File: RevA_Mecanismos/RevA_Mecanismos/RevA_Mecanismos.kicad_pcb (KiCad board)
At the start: 4 copper layers, 99.7 x 99.7 mm, 137 parts, among them IC1 MAX33040EAKA+T, J1 Conn_01x02_Socket, J10 Screw_Terminal_01x02, J11 Screw_Terminal_01x02, J12 Conn_01x08_Socket, J13 Conn_01x08_Socket, J14 Conn_01x02_Pin, J15 430450624, J16 Conn_01x07_Pin, J17 Conn_01x02_Pin, J18 Conn_01x02_Pin, J19 Conn_01x02_Pin, J2 PROG, J20 3557-2, J21 Conn_01x04_Pin, J22 Conn_01x04_Pin, J3 Conn_01x02_Pin, J4 430450224, J5 430450224, J6 430450224, J7 430450224, J8 3557-2, J9 3557-2, Q1 FDN335N, Q2 NDS352AP, Q3 IRF9540NSPBF, Q4 IRF9540NSPBF, Q5 IRF9540NSPBF, Q6 IRF9540NSPBF, SW1 SW_Push, U1 STM32L431RCTx, U2 R-78E3.3-1.0, U3 R-78E5.0-1.0, U4 IRF540SPBF, U5 IRF540SPBF, U6 IRF540SPBF, U7 IRF540SPBF, U8 TXB0104D, Y1 16MHz

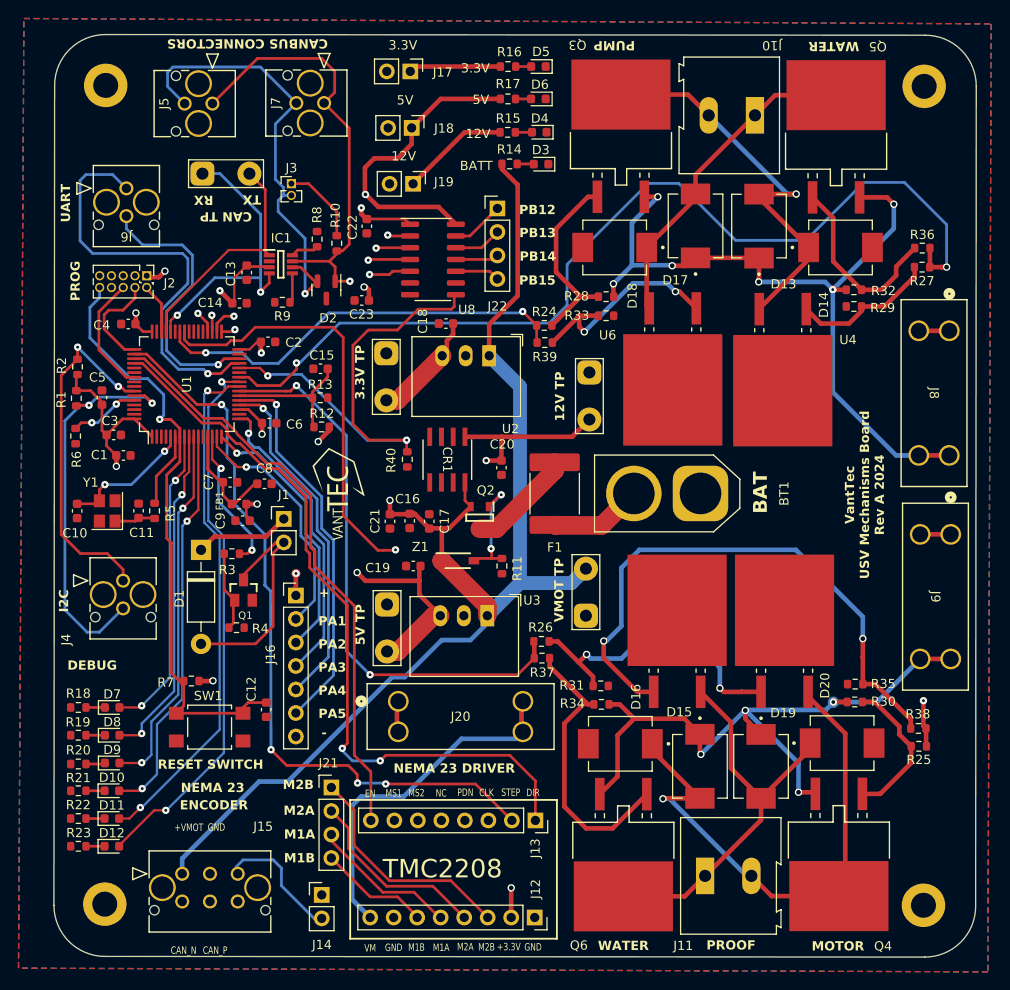
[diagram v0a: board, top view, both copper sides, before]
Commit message: Correct sizes for power connections between VBATT/VMOT, +12V, +5V, and +3V made
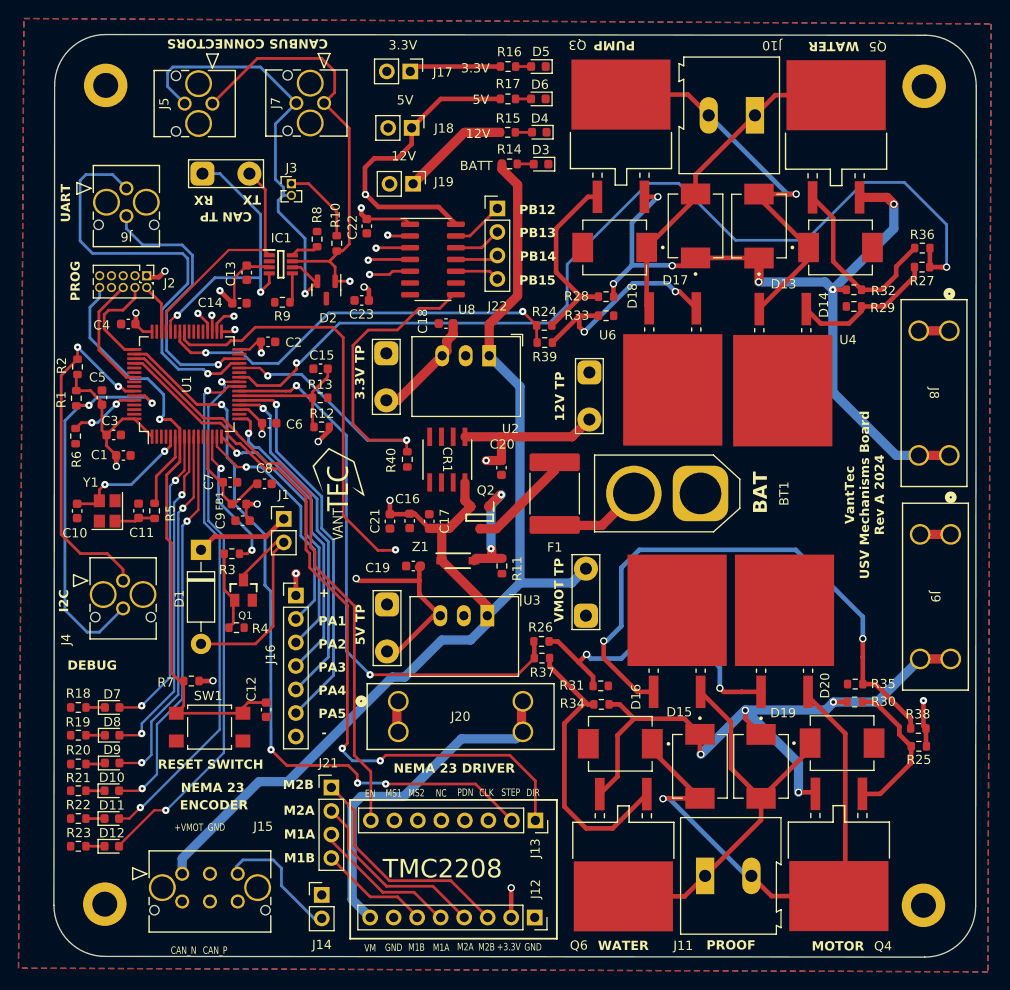
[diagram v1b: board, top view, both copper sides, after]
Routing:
- net Net-(J12-Pin_8): track 38.0 -> 37.3 mm
- net +12V: track 174.0 -> 173.4 mm
- net LEVEL_SHIFTER: track 51.8 -> 51.2 mm

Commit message: Corrections made to power supply routes and via sizes
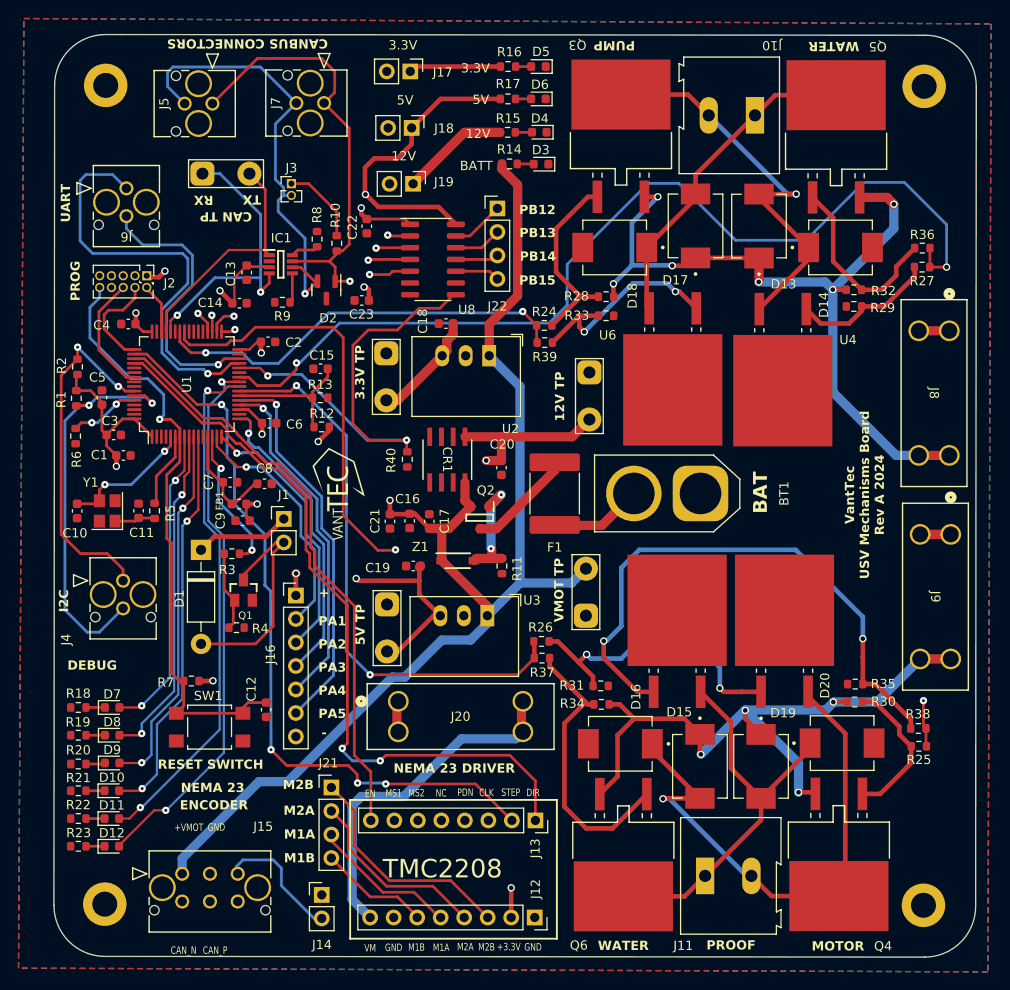
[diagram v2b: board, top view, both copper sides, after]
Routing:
- net WP_TIM1_CH2N: track 104.9 -> 104.3 mm
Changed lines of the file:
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@@
   (segment (start 111.05 64.675) (end 111.82 65.445) (width 0.5) (layer "F.Cu") (net 2))
   (segment (start 94.9998 115.1523) (end 95.0264 115.1257) (width 0.5) (layer "F.Cu") (net 2))
-  (segment (start 100.0593 78.3593) (end 100.2 78.5) (width 0.5) (layer "F.Cu") (net 2))
   (segment (start 98.625 96.025) (end 98.625 97.4493) (width 0.3) (layer "F.Cu") (net 2))
   (segment (start 100.2 79.65) (end 100.25 79.7) (width 0.5) (layer "F.Cu") (net 2))
@@
   (segment (start 98.625 97.4493) (end 99.0014 97.8257) (width 0.3) (layer "F.Cu") (net 2))
   (segment (start 100.175 78.475) (end 100.2 78.5) (width 0.5) (layer "F.Cu") (net 2))
-  (via (at 111.05 64.025) (size 0.8) (drill 0.3) (layers "F.Cu" "B.Cu") (net 2))
+  (via (at 111.05 64.025) (size 0.8) (drill 0.5) (layers "F.Cu" "B.Cu") (net 2))
   (via (at 95.0264 115.1257) (size 0.8) (drill 0.5) (layers "F.Cu" "B.Cu") (net 2))
   (via (at 89.8356 70.8547) (size 0.8) (drill 0.5) (layers "F.Cu" "B.Cu") (free) (net 2))
-  (via (at 104 103.525) (size 0.8) (drill 0.3) (layers "F.Cu" "B.Cu") (net 2))
-  (via (at 100.25 79.7) (size 0.8) (drill 0.3) (layers "F.Cu" "B.Cu") (free) (net 2))
-  (via (at 95.7764 72.9757) (size 0.8) (drill 0.3) (layers "F.Cu" "B.Cu") (free) (net 2))
+  (via (at 104 103.525) (size 0.8) (drill 0.5) (layers "F.Cu" "B.Cu") (net 2))
+  (via (at 100.25 79.7) (size 0.8) (drill 0.5) (layers "F.Cu" "B.Cu") (free) (net 2))
+  (via (at 95.7764 72.9757) (size 0.8) (drill 0.5) (layers "F.Cu" "B.Cu") (free) (net 2))
   (via (at 127.2514 137.5007) (size 0.8) (drill 0.5) (layers "F.Cu" "B.Cu") (net 2))
   (via (at 99.8 96.025) (size 0.8) (drill 0.5) (layers "F.Cu" "B.Cu") (free) (net 2))
@@
   (segment (start 116.4946 55.3838) (end 116.4946 57.1304) (width 0.5) (layer "F.Cu") (net 9))
   (via (at 110.5 104.075) (size 0.8) (drill 0.5) (layers "F.Cu" "B.Cu") (net 9))
-  (via (at 111.5 62.575) (size 0.8) (drill 0.4) (layers "F.Cu" "B.Cu") (net 9))
+  (via (at 111.5 62.575) (size 0.8) (drill 0.5) (layers "F.Cu" "B.Cu") (net 9))
   (via (at 111.35 72.575) (size 0.8) (drill 0.5) (layers "F.Cu" "B.Cu") (net 9))
   (segment (start 110.9 87.225) (end 111.75 88.075) (width 0.5) (layer "In1.Cu") (net 9))
@@
   (segment (start 126.225 88.7612) (end 133.8288 88.7612) (width 1) (layer "F.Cu") (net 40))
   (segment (start 114.9024 120.4919) (end 115.0524 120.6419) (width 1) (layer "F.Cu") (net 40))
-  (via (at 124.55 91.325) (size 0.8) (drill 0.4) (layers "F.Cu" "B.Cu") (net 40))
+  (via (at 124.55 91.325) (size 0.8) (drill 0.5) (layers "F.Cu" "B.Cu") (net 40))
   (segment (start 117.55 98.325) (end 113.65 98.325) (width 2) (layer "In1.Cu") (net 40))
   (segment (start 128.55 61.425) (end 132.1 64.975) (width 2) (layer "In1.Cu") (net 40))
@@
   (segment (start 144.65 70.275) (end 146.3231 70.275) (width 0.5) (layer "F.Cu") (net 48))
   (segment (start 147.172 69.4261) (end 154.0115 69.4261) (width 0.5) (layer "F.Cu") (net 48))
-  (via (at 162 72.855) (size 0.8) (drill 0.3) (layers "F.Cu" "B.Cu") (net 48))
+  (via (at 162 72.855) (size 0.8) (drill 0.5) (layers "F.Cu" "B.Cu") (net 48))
   (via (at 138.3 72.225) (size 0.8) (drill 0.5) (layers "F.Cu" "B.Cu") (net 48))
   (via (at 154 72.025) (size 0.8) (drill 0.5) (layers "F.Cu" "B.Cu") (net 48))
@@
   (via (at 147.75 123.075) (size 0.8) (drill 0.5) (layers "F.Cu" "B.Cu") (net 52))
   (via (at 152.55 118.325) (size 0.8) (drill 0.5) (layers "F.Cu" "B.Cu") (net 52))
-  (via (at 162.06 117.425) (size 0.8) (drill 0.4) (layers "F.Cu" "B.Cu") (net 52))
+  (via (at 162.06 117.425) (size 0.8) (drill 0.5) (layers "F.Cu" "B.Cu") (net 52))
   (segment (start 152.55 118.275) (end 152.55 118.275) (width 0.5) (layer "B.Cu") (net 52))
   (segment (start 158.3 127.175) (end 158.3 124.025) (width 1) (layer "B.Cu") (net 52))
@@
   (segment (start 112 114.475) (end 109.45 111.925) (width 0.3) (layer "B.Cu") (net 73))
   (segment (start 109.45 111.925) (end 109.45 88.625) (width 0.3) (layer "B.Cu") (net 73))
-  (segment (start 172.075 120.275) (end 172.075 122.1546) (width 0.5) (layer "F.Cu") (net 74))
+  (segment (start 172.075 120.275) (end 172.075 122.1546) (width 0.3) (layer "F.Cu") (net 74))
   (segment (start 109.1 78.025) (end 108 76.925) (width 0.3) (layer "F.Cu") (net 74))
-  (segment (start 171.8 117.275) (end 171.8 120) (width 0.5) (layer "F.Cu") (net 74))
+  (segment (start 171.8 117.275) (end 171.8 120) (width 0.3) (layer "F.Cu") (net 74))
   (segment (start 96.5 78.825) (end 92.49758 78.825) (width 0.3) (layer "F.Cu") (net 74))
   (segment (start 99.6 76.925) (end 98.15 78.375) (width 0.3) (layer "F.Cu") (net 74))
-  (segment (start 172.075 122.1546) (end 172.1258 122.2054) (width 0.5) (layer "F.Cu") (net 74))
+  (segment (start 172.075 122.1546) (end 172.1258 122.2054) (width 0.3) (layer "F.Cu") (net 74))
   (segment (start 109.1 97.275) (end 109.1 78.025) (width 0.3) (layer "F.Cu") (net 74))
   (segment (start 108 76.925) (end 99.6 76.925) (width 0.3) (layer "F.Cu") (net 74))
@@
   (segment (start 98.15 78.375) (end 96.95 78.375) (width 0.3) (layer "F.Cu") (net 74))
   (segment (start 114.7 101.025) (end 113.45 101.025) (width 0.3) (layer "F.Cu") (net 74))
-  (segment (start 171.8 120) (end 172.075 120.275) (width 0.5) (layer "F.Cu") (net 74))
+  (segment (start 171.8 120) (end 172.075 120.275) (width 0.3) (layer "F.Cu") (net 74))
   (segment (start 92.49758 78.825) (end 91.9478 78.27522) (width 0.3) (layer "F.Cu") (net 74))
   (via (at 171.8 117.275) (size 0.8) (drill 0.3) (layers "F.Cu" "B.Cu") (net 74))
@@
   (segment (start 114.75 100.975) (end 116.35 100.975) (width 0.3) (layer "In1.Cu") (net 74))
   (segment (start 99.8 83.225) (end 98.8971 82.3221) (width 0.3) (layer "F.Cu") (net 75))
-  (segment (start 172.5004 68.3676) (end 172.5004 70.3996) (width 0.5) (layer "F.Cu") (net 75))
-  (segment (start 174.3 70.425) (end 173.7 70.425) (width 0.5) (layer "F.Cu") (net 75))
+  (segment (start 172.5004 68.3676) (end 172.5004 70.3996) (width 0.3) (layer "F.Cu") (net 75))
   (segment (start 104.05 80.775) (end 104.05 81.475) (width 0.3) (layer "F.Cu") (net 75))
   (segment (start 102.3 83.225) (end 99.8 83.225) (width 0.3) (layer "F.Cu") (net 75))
   (segment (start 98.8971 82.3221) (end 97.8728 82.3221) (width 0.3) (layer "F.Cu") (net 75))
   (segment (start 104.05 81.475) (end 102.3 83.225) (width 0.3) (layer "F.Cu") (net 75))
-  (segment (start 172.475 70.425) (end 174.3 70.425) (width 0.5) (layer "F.Cu") (net 75))
+  (segment (start 172.475 70.425) (end 174.3 70.425) (width 0.3) (layer "F.Cu") (net 75))
   (via (at 174.3 70.425) (size 0.8) (drill 0.5) (layers "F.Cu" "B.Cu") (net 75))
   (via (at 104.05 80.775) (size 0.8) (drill 0.3) (layers "F.Cu" "B.Cu") (net 75))

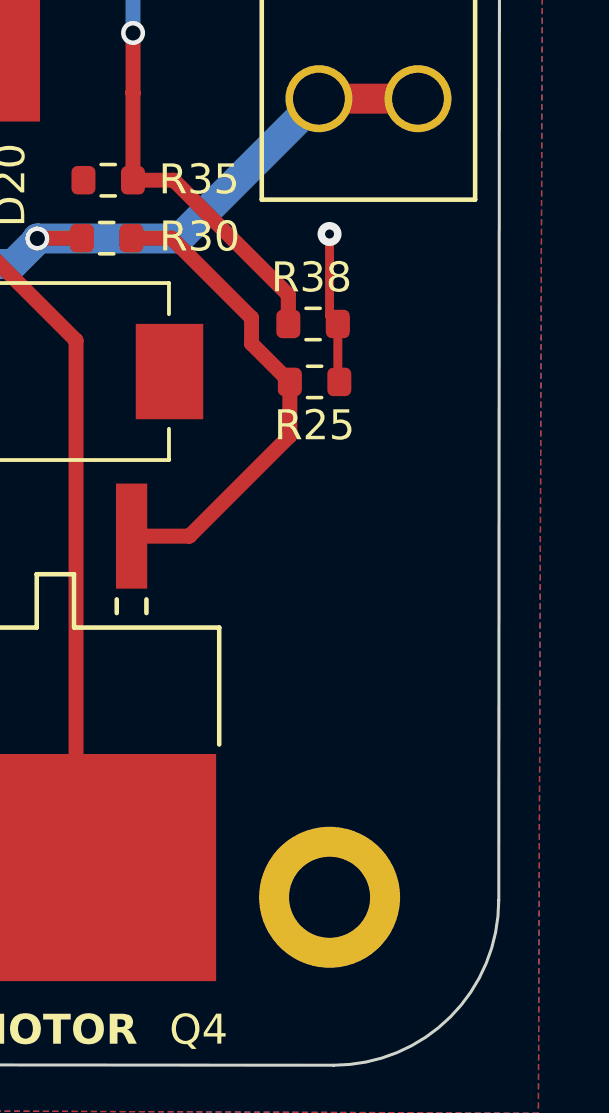
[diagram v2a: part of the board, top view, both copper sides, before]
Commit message: Name of developer added to PCB
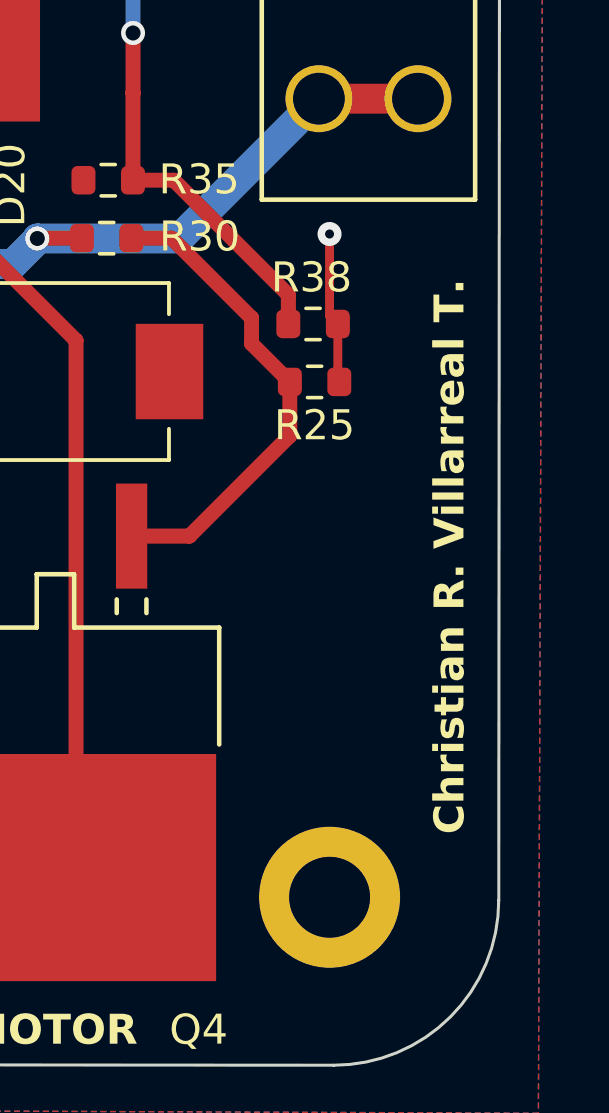
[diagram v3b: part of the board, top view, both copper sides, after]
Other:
- board text added: "Christian R. Villarreal T."
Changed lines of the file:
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@@
     (effects (font (size 0.8 0.6) (thickness 0.125)))
+  )
+  (gr_text "Christian R. Villarreal T." (at 175.8 128.025 90) (layer "F.SilkS")
+    (effects (font (size 1 1) (thickness 0.25) bold))
   )
   (gr_text "BATT" (at 125.2562 59.477) (layer "F.SilkS")

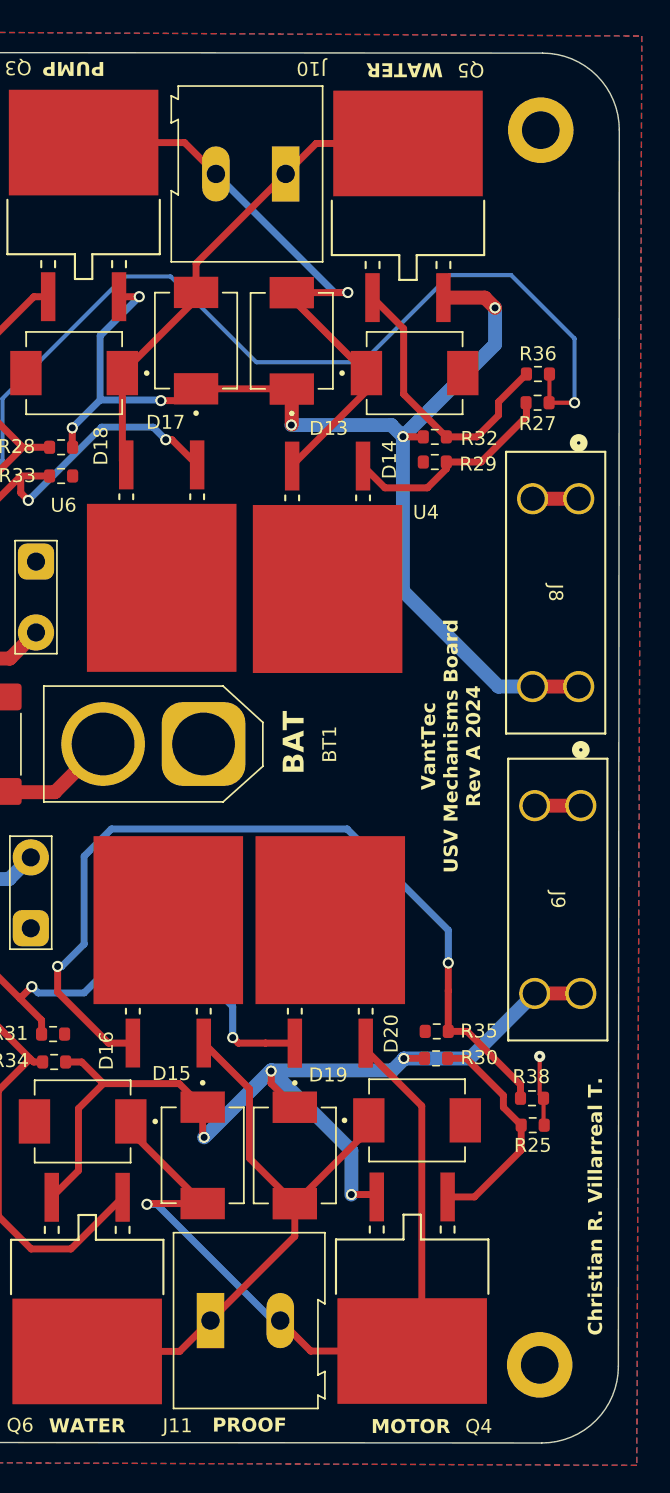
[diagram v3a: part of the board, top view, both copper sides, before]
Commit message: Replacement of screw terminals for molex connectors
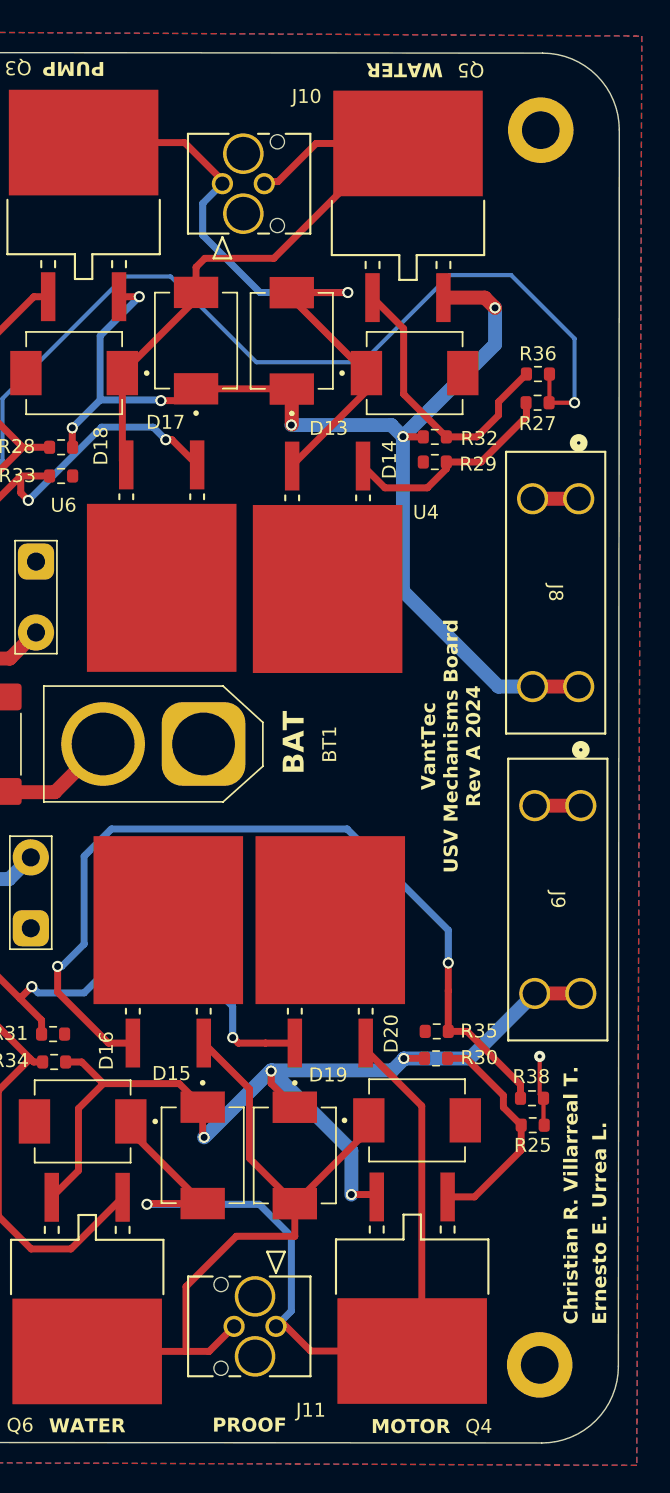
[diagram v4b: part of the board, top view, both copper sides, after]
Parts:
- J10, J11: value Screw_Terminal_01x02 -> 430450224; footprint TerminalBlock:TerminalBlock_Altech_AK300-2_P5.00mm -> MolexConnectors:CON_430450224_MOL
- moved J11 4.71 mm to (152.9, 136.6), turned to 90 degrees
- moved J10 4.59 mm to (149.1, 54.7), turned to -90 degrees
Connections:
- J10 pad 1: WP_- -> WP_+
- J10 pad 2: WP_+ -> WP_-
- J11 pad 1: WPM_- -> WPM_+
- J11 pad 2: WPM_+ -> WPM_-
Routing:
- net WP_-: track 35.5 -> 47.0 mm
- net WPM_-: track 43.0 -> 49.9 mm
- net WPM_+: track 59.6 -> 65.3 mm
- net WP_+: track 44.6 -> 48.9 mm
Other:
- board text added: "Ernesto E. Urrea L."
